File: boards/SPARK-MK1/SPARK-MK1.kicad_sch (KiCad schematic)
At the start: 64 parts, among them J1 Screw_Terminal_01x02, J101 Conn_01x03_Pin, J102 Screw_Terminal_01x02, J103 Screw_Terminal_01x02, J104 Conn_01x03_Pin, J105 Conn_01x03_Pin, J106 Screw_Terminal_01x02, J107 Screw_Terminal_01x02, J109 Conn_01x04_Pin, J110 Conn_01x02_Pin, J111 Conn_01x04_Pin, J112 Conn_01x04_Pin, J113 Conn_01x03_Pin, J2 Screw_Terminal_01x02, J3 Screw_Terminal_01x02, J4 Screw_Terminal_01x02, U1 AD5252BRUZ1, U101 AD5252BRUZ1, U2 Teensy4.1_bare, U5 TPS25947, U6 TPS25947, U7 TPS25947, U8 TPS25947

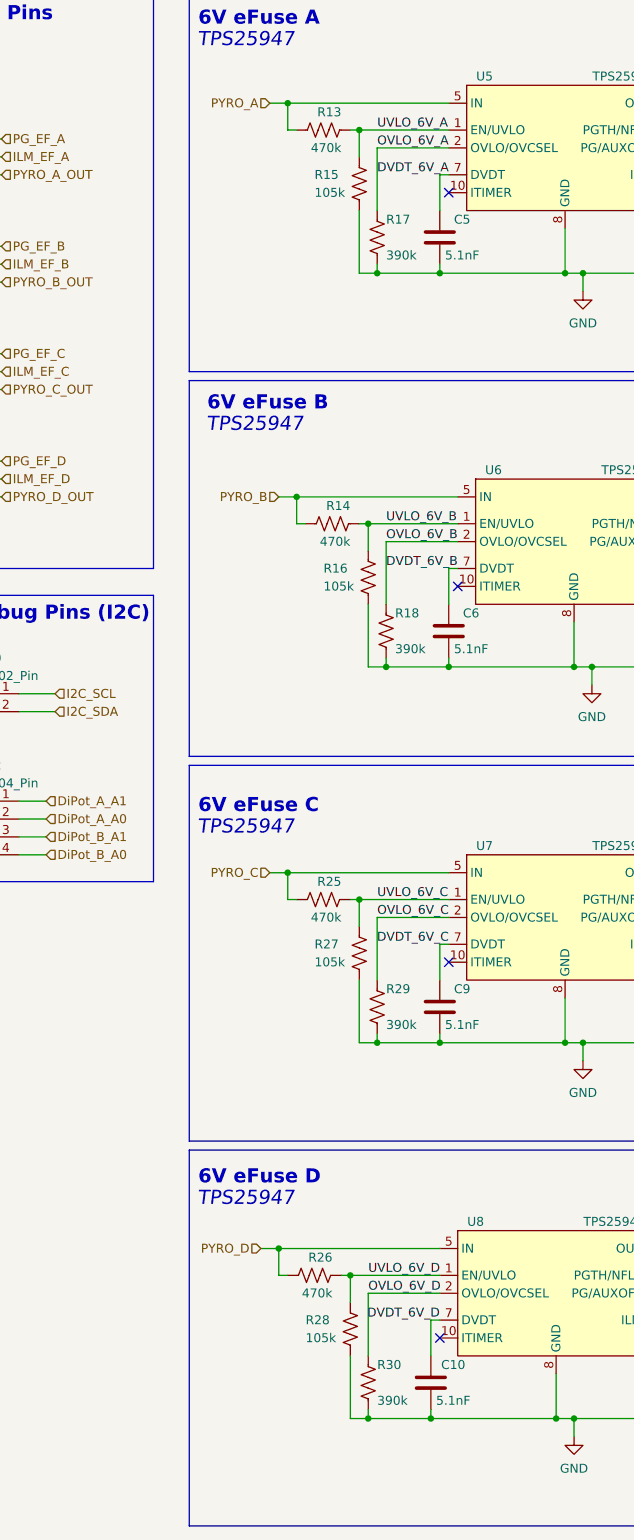
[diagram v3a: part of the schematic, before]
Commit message: Adding polarized capacitor to each e-fise. See: TPS25947 datasheet
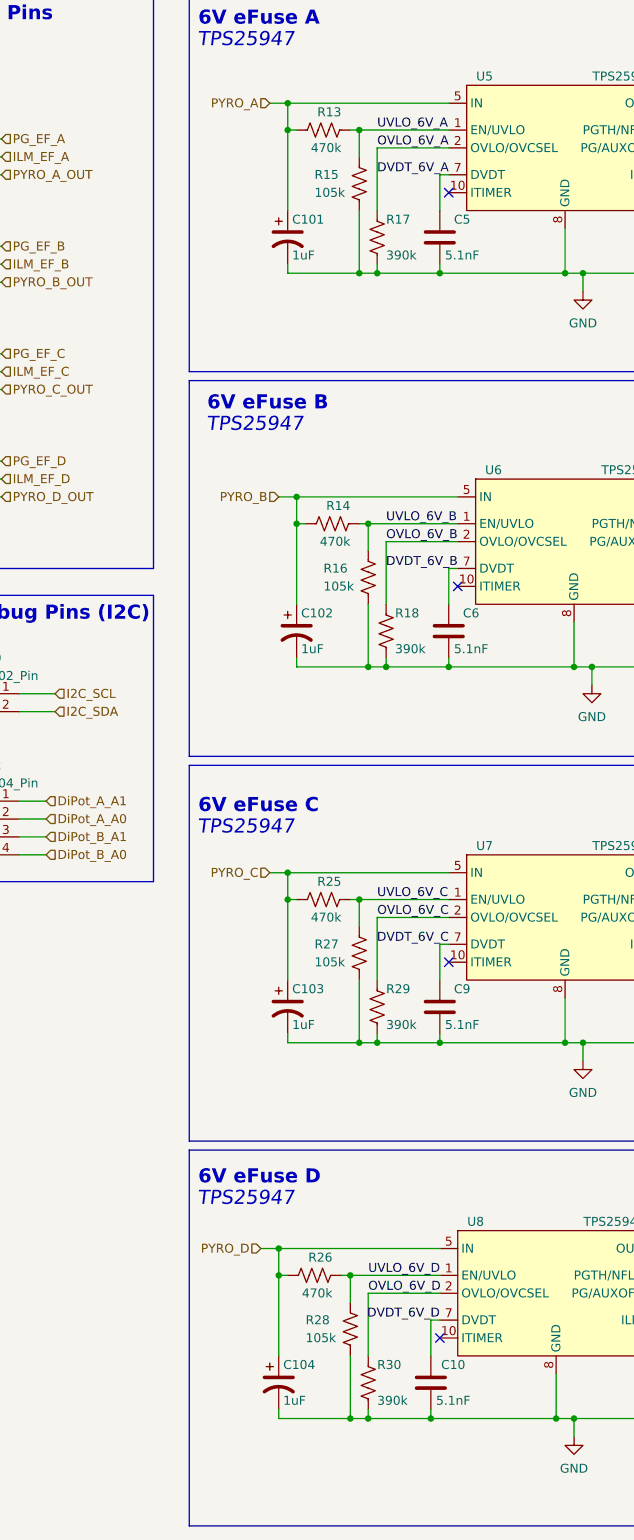
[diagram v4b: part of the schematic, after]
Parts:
- added C101, C102, C103, C104: 1uF, Capacitor_SMD:C_0603_1608Metric, symbol Device:C_Polarized_US
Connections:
- net GND: now also C101.2, C102.2, C103.2, C104.2
- net PYRO_A: now also C101.1
- net PYRO_B: now also C102.1
- net PYRO_C: now also C103.1
- net PYRO_D: now also C104.1
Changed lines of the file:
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@@
   (junction (at 364.49 195.58) (diameter 0) (color 0 0 0 0)
   )
+  (junction (at 306.07 215.9) (diameter 0) (color 0 0 0 0)
+  )
+  (junction (at 298.45 88.9) (diameter 0) (color 0 0 0 0)
+  )
   (junction (at 298.45 85.09) (diameter 0) (color 0 0 0 0)
   )
   (junction (at 320.04 109.22) (diameter 0) (color 0 0 0 0)
   )
+  (junction (at 307.34 162.56) (diameter 0) (color 0 0 0 0)
+  )
   (junction (at 336.55 53.34) (diameter 0) (color 0 0 0 0)
   )
@@
   (junction (at 377.19 88.9) (diameter 0) (color 0 0 0 0)
   )
+  (junction (at 308.61 109.22) (diameter 0) (color 0 0 0 0)
+  )
   (junction (at 375.92 29.21) (diameter 0) (color 0 0 0 0)
   )
@@
   (junction (at 353.06 148.59) (diameter 0) (color 0 0 0 0)
   )
+  (junction (at 307.34 53.34) (diameter 0) (color 0 0 0 0)
+  )
   (junction (at 351.79 201.93) (diameter 0) (color 0 0 0 0)
   )
@@
   (junction (at 308.61 88.9) (diameter 0) (color 0 0 0 0)
   )
+  (junction (at 295.91 195.58) (diameter 0) (color 0 0 0 0)
+  )
   (junction (at 335.28 215.9) (diameter 0) (color 0 0 0 0)
   )
@@
   (junction (at 30.48 66.04) (diameter 0) (color 0 0 0 0)
   )
+  (junction (at 297.18 142.24) (diameter 0) (color 0 0 0 0)
+  )
   (junction (at 365.76 162.56) (diameter 0) (color 0 0 0 0)
   )
@@
   (junction (at 101.6 72.39) (diameter 0) (color 0 0 0 0)
   )
+  (junction (at 297.18 33.02) (diameter 0) (color 0 0 0 0)
+  )
   (junction (at 353.06 144.78) (diameter 0) (color 0 0 0 0)
   )
@@
   (no_connect (at 110.49 125.73))
   (no_connect (at 54.61 153.67))
+  (wire (pts (xy 306.07 215.9) (xy 295.91 215.9))
+    (stroke (width 0) (type default))
+  )
   (wire (pts (xy 318.77 39.37) (xy 320.04 39.37))
     (stroke (width 0) (type default))
@@
     (stroke (width 0) (type default))
   )
+  (wire (pts (xy 295.91 195.58) (xy 295.91 207.01))
+    (stroke (width 0) (type default))
+  )
   (wire (pts (xy 309.88 161.29) (xy 309.88 162.56))
     (stroke (width 0) (type default))
@@
     (stroke (width 0) (type default))
   )
+  (wire (pts (xy 295.91 215.9) (xy 295.91 214.63))
+    (stroke (width 0) (type default))
+  )
   (wire (pts (xy 320.04 35.56) (xy 309.88 35.56))
     (stroke (width 0) (type default))
@@
     (stroke (width 0) (type default))
   )
+  (wire (pts (xy 297.18 53.34) (xy 307.34 53.34))
+    (stroke (width 0) (type default))
+  )
   (wire (pts (xy 365.76 142.24) (xy 367.03 142.24))
     (stroke (width 0) (type default))
   )
+  (wire (pts (xy 298.45 88.9) (xy 298.45 100.33))
+    (stroke (width 0) (type default))
+  )
   (wire (pts (xy 351.79 29.21) (xy 375.92 29.21))
     (stroke (width 0) (type default))
@@
     (stroke (width 0) (type default))
   )
+  (wire (pts (xy 297.18 162.56) (xy 307.34 162.56))
+    (stroke (width 0) (type default))
+  )
   (wire (pts (xy 49.53 173.99) (xy 54.61 173.99))
     (stroke (width 0) (type default))
@@
     (stroke (width 0) (type default))
   )
+  (wire (pts (xy 298.45 107.95) (xy 298.45 109.22))
+    (stroke (width 0) (type default))
+  )
   (wire (pts (xy 339.09 53.34) (xy 339.09 55.88))
     (stroke (width 0) (type default))
@@
     (stroke (width 0) (type default))
   )
+  (wire (pts (xy 297.18 33.02) (xy 297.18 44.45))
+    (stroke (width 0) (type default))
+  )
   (wire (pts (xy 307.34 44.45) (xy 307.34 53.34))
     (stroke (width 0) (type default))
@@
     (stroke (width 0) (type default))
   )
+  (wire (pts (xy 297.18 52.07) (xy 297.18 53.34))
+    (stroke (width 0) (type default))
+  )
   (wire (pts (xy 52.07 140.97) (xy 54.61 140.97))
     (stroke (width 0) (type default))
@@
     (stroke (width 0) (type default))
   )
+  (wire (pts (xy 297.18 161.29) (xy 297.18 162.56))
+    (stroke (width 0) (type default))
+  )
   (wire (pts (xy 101.6 36.83) (xy 105.41 36.83))
     (stroke (width 0) (type default))
@@
     (stroke (width 0) (type default))
   )
+  (wire (pts (xy 297.18 142.24) (xy 297.18 153.67))
+    (stroke (width 0) (type default))
+  )
   (wire (pts (xy 140.97 59.69) (xy 143.51 59.69))
     (stroke (width 0) (type default))
@@
     (stroke (width 0) (type default))
   )
+  (wire (pts (xy 298.45 109.22) (xy 308.61 109.22))
+    (stroke (width 0) (type default))
+  )
   (wire (pts (xy 306.07 215.9) (xy 308.61 215.9))
     (stroke (width 0) (type default))
@@
     )
   )
+  (symbol (lib_id "Device:C_Polarized_US") (at 297.18 48.26 0) (unit 1)
+    (in_bom yes) (on_board yes) (dnp no)
+    (property "Reference" "C101" (at 297.815 45.72 0)
+      (effects (font (size 1.27 1.27)) (justify left))
+    )
+    (property "Value" "1uF" (at 297.815 50.8 0)
+      (effects (font (size 1.27 1.27)) (justify left))
+    )
+    (property "Footprint" "Capacitor_SMD:C_0603_1608Metric" (at 297.18 48.26 0)
+      (effects (font (size 1.27 1.27)) hide)
+    )
+    (property "Datasheet" "~" (at 297.18 48.26 0)
+      (effects (font (size 1.27 1.27)) hide)
+    )
+    (pin "1")
+    (pin "2")
+    (instances
+      (project "SPARK-MK1"
+        (path "/9ed31ef1-850d-4612-a113-88d01cf221f5"
+          (reference "C101") (unit 1)
+        )
+      )
+    )
+  )
   (symbol (lib_id "Device:R_US") (at 308.61 96.52 0) (unit 1)
     (in_bom yes) (on_board yes) (dnp no)
@@
     )
   )
+  (symbol (lib_id "Device:C_Polarized_US") (at 295.91 210.82 0) (unit 1)
+    (in_bom yes) (on_board yes) (dnp no)
+    (property "Reference" "C104" (at 296.545 208.28 0)
+      (effects (font (size 1.27 1.27)) (justify left))
+    )
+    (property "Value" "1uF" (at 296.545 213.36 0)
+      (effects (font (size 1.27 1.27)) (justify left))
+    )
+    (property "Footprint" "Capacitor_SMD:C_0603_1608Metric" (at 295.91 210.82 0)
+      (effects (font (size 1.27 1.27)) hide)
+    )
+    (property "Datasheet" "~" (at 295.91 210.82 0)
+      (effects (font (size 1.27 1.27)) hide)
+    )
+    (pin "1")
+    (pin "2")
+    (instances
+      (project "SPARK-MK1"
+        (path "/9ed31ef1-850d-4612-a113-88d01cf221f5"
+          (reference "C104") (unit 1)
+        )
+      )
+    )
+  )
   (symbol (lib_id "Power_eFuse:TPS25947") (at 335.28 200.66 0) (unit 1)
     (in_bom yes) (on_board yes) (dnp no) (fields_autoplaced)
@@
     )
   )
+  (symbol (lib_id "Device:C_Polarized_US") (at 298.45 104.14 0) (unit 1)
+    (in_bom yes) (on_board yes) (dnp no)
+    (property "Reference" "C102" (at 299.085 101.6 0)
+      (effects (font (size 1.27 1.27)) (justify left))
+    )
+    (property "Value" "1uF" (at 299.085 106.68 0)
+      (effects (font (size 1.27 1.27)) (justify left))
+    )
+    (property "Footprint" "Capacitor_SMD:C_0603_1608Metric" (at 298.45 104.14 0)
+      (effects (font (size 1.27 1.27)) hide)
+    )
+    (property "Datasheet" "~" (at 298.45 104.14 0)
+      (effects (font (size 1.27 1.27)) hide)
+    )
+    (pin "1")
+    (pin "2")
+    (instances
+      (project "SPARK-MK1"
+        (path "/9ed31ef1-850d-4612-a113-88d01cf221f5"
+          (reference "C102") (unit 1)
+        )
+      )
+    )
+  )
   (symbol (lib_id "Device:R_US") (at 307.34 149.86 0) (unit 1)
     (in_bom yes) (on_board yes) (dnp no)
@@
         )
       )
+    )
+  )
+  (symbol (lib_id "Device:C_Polarized_US") (at 297.18 157.48 0) (unit 1)
+    (in_bom yes) (on_board yes) (dnp no)
+    (property "Reference" "C103" (at 297.815 154.94 0)
+      (effects (font (size 1.27 1.27)) (justify left))
+    )
+    (property "Value" "1uF" (at 297.815 160.02 0)
+      (effects (font (size 1.27 1.27)) (justify left))
+    )
+    (property "Footprint" "Capacitor_SMD:C_0603_1608Metric" (at 297.18 157.48 0)
+      (effects (font (size 1.27 1.27)) hide)
+    )
+    (property "Datasheet" "~" (at 297.18 157.48 0)
+      (effects (font (size 1.27 1.27)) hide)
+    )
+    (pin "1")
+    (pin "2")
+    (instances
+      (project "SPARK-MK1"
+        (path "/9ed31ef1-850d-4612-a113-88d01cf221f5"
+          (reference "C103") (unit 1)
+        )
+      )

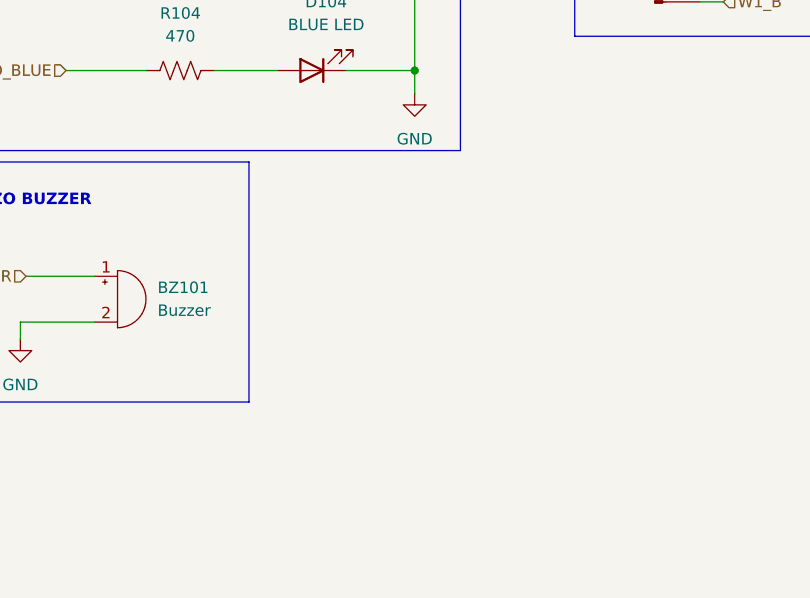
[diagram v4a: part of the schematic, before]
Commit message: added mounting holes
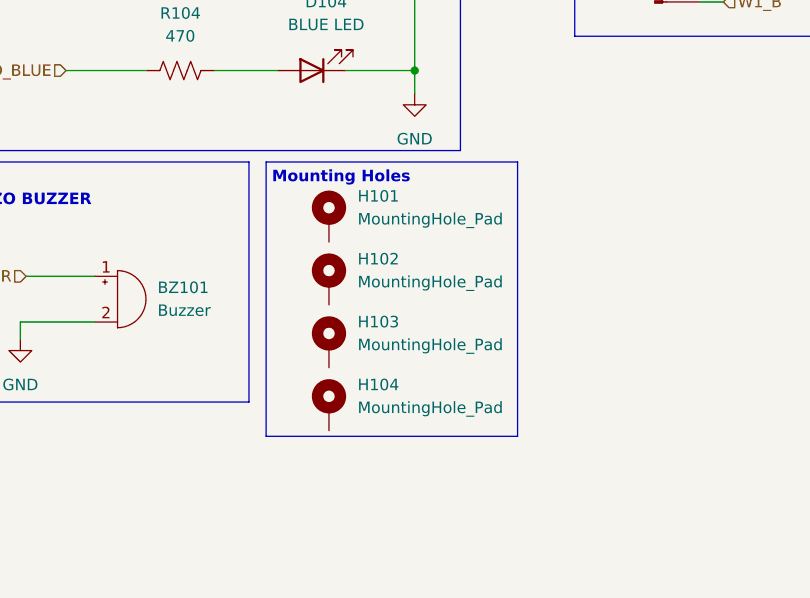
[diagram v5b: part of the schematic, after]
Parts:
- added H101, H102, H103, H104: MountingHole_Pad, MountingHole:MountingHole_3.2mm_M3_Pad_Via, symbol Mechanical:MountingHole_Pad
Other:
- note added: "Mounting Holes"
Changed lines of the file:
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@@
     (stroke (width 0) (type default))
+  )
+  (rectangle (start 181.61 153.67) (end 209.55 184.15)
+    (stroke (width 0) (type default))
+    (fill (type none))
   )
   (rectangle (start 38.735 198.12) (end 38.735 198.12)
@@
     (effects (font (size 1.5 1.5) italic) (justify left bottom))
   )
+  (text "Mounting Holes\n" (at 182.245 156.21 0)
+    (effects (font (face "KiCad Font") (size 1.27 1.27) (thickness 0.254) bold) (justify left bottom))
+  )
   (text "CURRENT LIMIT 5.5A\nOVLO 13.8V\nUVLO 6.5V" (at 403.86 21.59 0)
     (effects (font (size 1.27 1.27)) (justify right bottom))
@@
     (effects (font (size 1.27 1.27)) (justify left))
   )
+  (symbol (lib_id "Mechanical:MountingHole_Pad") (at 188.595 167.005 0) (unit 1)
+    (in_bom yes) (on_board yes) (dnp no) (fields_autoplaced)
+    (property "Reference" "H102" (at 191.77 164.465 0)
+      (effects (font (size 1.27 1.27)) (justify left))
+    )
+    (property "Value" "MountingHole_Pad" (at 191.77 167.005 0)
+      (effects (font (size 1.27 1.27)) (justify left))
+    )
+    (property "Footprint" "MountingHole:MountingHole_3.2mm_M3_Pad_Via" (at 188.595 167.005 0)
+      (effects (font (size 1.27 1.27)) hide)
+    )
+    (property "Datasheet" "~" (at 188.595 167.005 0)
+      (effects (font (size 1.27 1.27)) hide)
+    )
+    (pin "1")
+    (instances
+      (project "SPARK-MK1"
+        (path "/9ed31ef1-850d-4612-a113-88d01cf221f5"
+          (reference "H102") (unit 1)
+        )
+      )
+    )
+  )
   (symbol (lib_id "Device:C") (at 317.5 210.82 0) (unit 1)
     (in_bom yes) (on_board yes) (dnp no)
@@
         (path "/e63e39d7-6ac0-4ffd-8aa3-1841a4541b55"
           (reference "R103") (unit 1)
+        )
+      )
+    )
+  )
+  (symbol (lib_id "Mechanical:MountingHole_Pad") (at 188.595 160.02 0) (unit 1)
+    (in_bom yes) (on_board yes) (dnp no) (fields_autoplaced)
+    (property "Reference" "H101" (at 191.77 157.48 0)
+      (effects (font (size 1.27 1.27)) (justify left))
+    )
+    (property "Value" "MountingHole_Pad" (at 191.77 160.02 0)
+      (effects (font (size 1.27 1.27)) (justify left))
+    )
+    (property "Footprint" "MountingHole:MountingHole_3.2mm_M3_Pad_Via" (at 188.595 160.02 0)
+      (effects (font (size 1.27 1.27)) hide)
+    )
+    (property "Datasheet" "~" (at 188.595 160.02 0)
+      (effects (font (size 1.27 1.27)) hide)
+    )
+    (pin "1")
+    (instances
+      (project "SPARK-MK1"
+        (path "/9ed31ef1-850d-4612-a113-88d01cf221f5"
+          (reference "H101") (unit 1)
         )
       )
@@
     )
   )
+  (symbol (lib_id "Mechanical:MountingHole_Pad") (at 188.595 173.99 0) (unit 1)
+    (in_bom yes) (on_board yes) (dnp no) (fields_autoplaced)
+    (property "Reference" "H103" (at 191.77 171.45 0)
+      (effects (font (size 1.27 1.27)) (justify left))
+    )
+    (property "Value" "MountingHole_Pad" (at 191.77 173.99 0)
+      (effects (font (size 1.27 1.27)) (justify left))
+    )
+    (property "Footprint" "MountingHole:MountingHole_3.2mm_M3_Pad_Via" (at 188.595 173.99 0)
+      (effects (font (size 1.27 1.27)) hide)
+    )
+    (property "Datasheet" "~" (at 188.595 173.99 0)
+      (effects (font (size 1.27 1.27)) hide)
+    )
+    (pin "1")
+    (instances
+      (project "SPARK-MK1"
+        (path "/9ed31ef1-850d-4612-a113-88d01cf221f5"
+          (reference "H103") (unit 1)
+        )
+      )
+    )
+  )
   (symbol (lib_id "Device:R_US") (at 308.61 96.52 0) (unit 1)
     (in_bom yes) (on_board yes) (dnp no)
@@
     )
     (pin "1")
+    (pin "2")
+    (pin "3")
     (pin "4")
-    (pin "2")
-    (pin "3")
     (instances
       (project "SPARK-MK1"
@@
     )
     (pin "1")
+    (pin "2")
+    (pin "3")
     (pin "4")
+    (instances
+      (project "SPARK-MK1"
+        (path "/9ed31ef1-850d-4612-a113-88d01cf221f5"
+          (reference "J112") (unit 1)
+        )
+      )
+    )
+  )
+  (symbol (lib_id "Connector:Conn_01x03_Pin") (at 246.38 82.55 0) (unit 1)
+    (in_bom yes) (on_board yes) (dnp no) (fields_autoplaced)
+    (property "Reference" "J105" (at 247.015 74.93 0)
+      (effects (font (size 1.27 1.27)))
+    )
+    (property "Value" "Conn_01x03_Pin" (at 247.015 77.47 0)
+      (effects (font (size 1.27 1.27)))
+    )
+    (property "Footprint" "Connector_PinHeader_2.54mm:PinHeader_1x03_P2.54mm_Vertical" (at 246.38 82.55 0)
+      (effects (font (size 1.27 1.27)) hide)
+    )
+    (property "Datasheet" "~" (at 246.38 82.55 0)
+      (effects (font (size 1.27 1.27)) hide)
+    )
+    (pin "1")
     (pin "2")
     (pin "3")
-    (instances
-      (project "SPARK-MK1"
-        (path "/9ed31ef1-850d-4612-a113-88d01cf221f5"
-          (reference "J112") (unit 1)
-        )
-      )
-    )
-  )
-  (symbol (lib_id "Connector:Conn_01x03_Pin") (at 246.38 82.55 0) (unit 1)
-    (in_bom yes) (on_board yes) (dnp no) (fields_autoplaced)
-    (property "Reference" "J105" (at 247.015 74.93 0)
-      (effects (font (size 1.27 1.27)))
-    )
-    (property "Value" "Conn_01x03_Pin" (at 247.015 77.47 0)
-      (effects (font (size 1.27 1.27)))
-    )
-    (property "Footprint" "Connector_PinHeader_2.54mm:PinHeader_1x03_P2.54mm_Vertical" (at 246.38 82.55 0)
-      (effects (font (size 1.27 1.27)) hide)
-    )
-    (property "Datasheet" "~" (at 246.38 82.55 0)
-      (effects (font (size 1.27 1.27)) hide)
-    )
-    (pin "3")
-    (pin "1")
-    (pin "2")
     (instances
       (project "SPARK-MK1"
@@
       (effects (font (size 1.27 1.27)) hide)
     )
+    (pin "1")
+    (pin "2")
     (pin "3")
-    (pin "1")
-    (pin "2")
     (instances
       (project "SPARK-MK1"
@@
       (effects (font (size 1.27 1.27)) hide)
     )
+    (pin "1")
+    (pin "2")
     (pin "3")
-    (pin "1")
-    (pin "2")
     (instances
       (project "SPARK-MK1"
@@
       (effects (font (size 1.27 1.27)) hide)
     )
+    (pin "1")
+    (pin "2")
     (pin "3")
-    (pin "1")
-    (pin "2")
     (instances
       (project "SPARK-MK1"
@@
     )
     (pin "1")
+    (pin "2")
+    (pin "3")
     (pin "4")
-    (pin "2")
-    (pin "3")
     (instances
       (project "SPARK-MK1"
@@
         )
       )
+    )
+  )
+  (symbol (lib_id "Mechanical:MountingHole_Pad") (at 188.595 180.975 0) (unit 1)
+    (in_bom yes) (on_board yes) (dnp no) (fields_autoplaced)
+    (property "Reference" "H104" (at 191.77 178.435 0)
+      (effects (font (size 1.27 1.27)) (justify left))
+    )
+    (property "Value" "MountingHole_Pad" (at 191.77 180.975 0)
+      (effects (font (size 1.27 1.27)) (justify left))
+    )
+    (property "Footprint" "MountingHole:MountingHole_3.2mm_M3_Pad_Via" (at 188.595 180.975 0)
+      (effects (font (size 1.27 1.27)) hide)
+    )
+    (property "Datasheet" "~" (at 188.595 180.975 0)
+      (effects (font (size 1.27 1.27)) hide)
+    )
+    (pin "1")
+    (instances
+      (project "SPARK-MK1"
+        (path "/9ed31ef1-850d-4612-a113-88d01cf221f5"
+          (reference "H104") (unit 1)
+        )
+      )

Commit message: Routed
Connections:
- net 3v3 is gone; now on net 3V3: U2.15 (3V3), U2.46 (3V3)
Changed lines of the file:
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@@
     (effects (font (size 1.27 1.27)) (justify left))
   )
-  (hierarchical_label "3v3" (shape output) (at 48.26 161.29 180) (fields_autoplaced)
+  (hierarchical_label "3V3" (shape output) (at 48.26 161.29 180) (fields_autoplaced)
     (effects (font (size 1.27 1.27)) (justify right))
   )
@@
     (effects (font (size 1.27 1.27)) (justify right))
   )
-  (hierarchical_label "3v3" (shape output) (at 116.84 130.81 0) (fields_autoplaced)
+  (hierarchical_label "3V3" (shape output) (at 116.84 130.81 0) (fields_autoplaced)
     (effects (font (size 1.27 1.27)) (justify left))
   )
